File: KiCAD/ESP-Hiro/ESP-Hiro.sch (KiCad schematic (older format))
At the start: 69 parts, among them J1 Conn_Q1, J2 Conn_Q2, J3 Conn_Q3, J4 Conn_Q4, J5 Conn_Q5, J6 Conn_ADC, J7 Korean Hroparts TYPE-C-31-M-12, Q1 AO3400A, Q2 AO3400A, Q3 AO3400A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

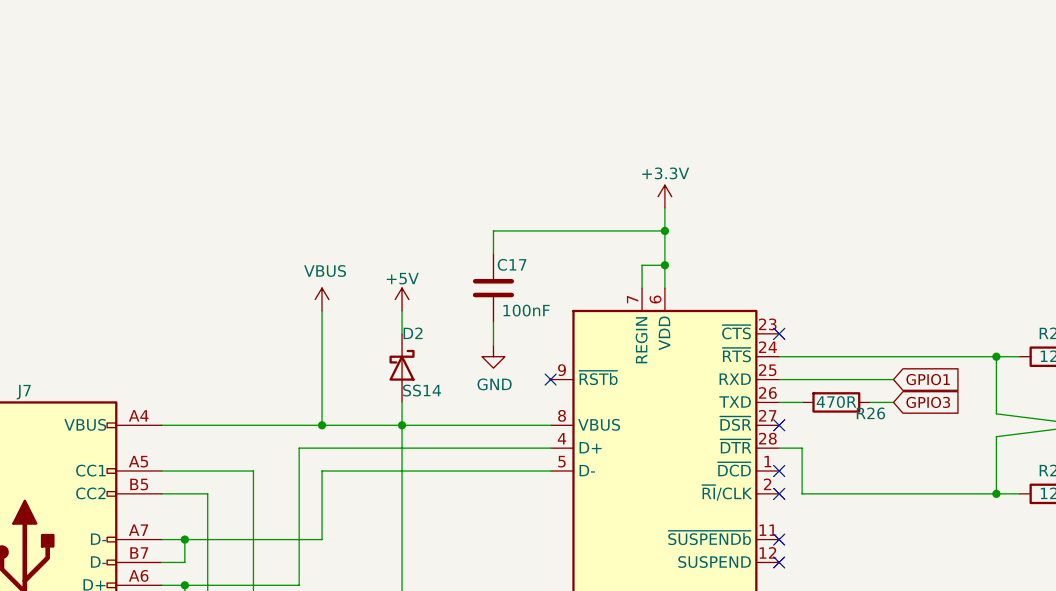
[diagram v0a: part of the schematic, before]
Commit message: configure CP2102 as only USB powered
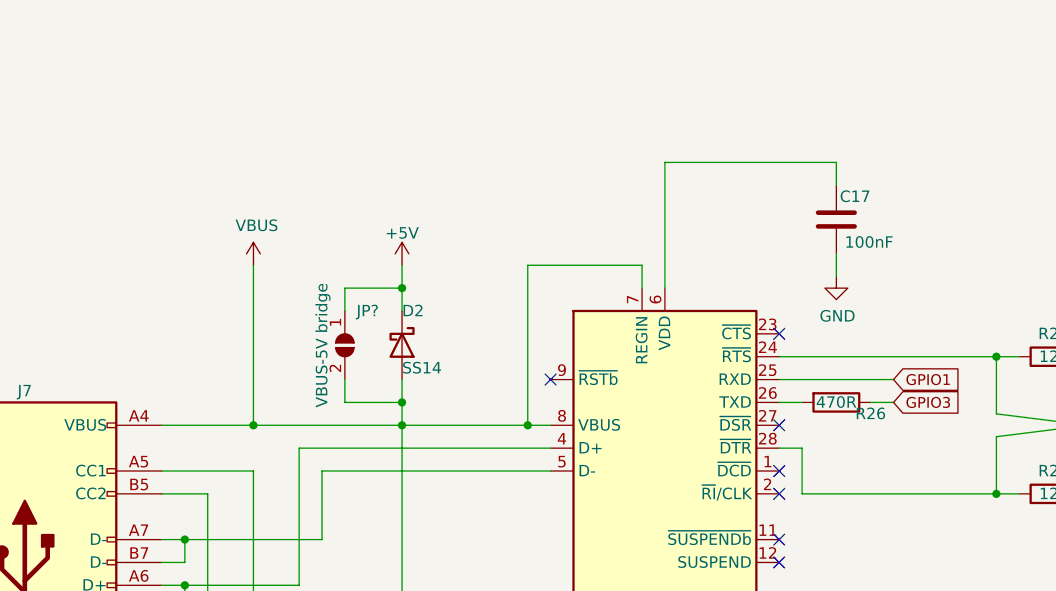
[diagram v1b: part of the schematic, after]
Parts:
- added JP?: VBUS-5V bridge, Jumper:SolderJumper-2_P1.3mm_Open_TrianglePad1.0x1.5mm, symbol Jumper:SolderJumper_2_Open
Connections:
- net +3V3: no longer C17.2, U5.6 (VDD), U5.7 (REGIN)
- net +5V: now also JP?.1 (A)
- net VBUS: now also U5.7 (REGIN), JP?.2 (B)
- new net: C17.2, U5.6 (VDD)
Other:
- moved on the sheet: C17, D2
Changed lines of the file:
@@
 	1200 6750 1200 6850
 Wire Wire Line
-	2100 5150 2800 5150
+	2100 5150 2500 5150
 Wire Wire Line
 	2100 5650 2200 5650
@@
 L power:VBUS #PWR0102
 U 1 1 602A343F
-P 2800 4650
-F 0 "#PWR0102" H 2800 4500 50  0001 C CNN
-F 1 "VBUS" H 2815 4823 50  0000 C CNN
-F 2 "" H 2800 4650 50  0001 C CNN
-F 3 "" H 2800 4650 50  0001 C CNN
-	1    2800 4650
+P 2500 4450
+F 0 "#PWR0102" H 2500 4300 50  0001 C CNN
+F 1 "VBUS" H 2515 4623 50  0000 C CNN
+F 2 "" H 2500 4450 50  0001 C CNN
+F 3 "" H 2500 4450 50  0001 C CNN
+	1    2500 4450
 	1    0    0    -1
 $EndComp
 Connection ~ 3150 5150
 Wire Wire Line
-	3150 5150 3800 5150
-$Comp
-L power:+3.3V #PWR?
-U 1 1 602B1B9F
-P 4300 4200
-AR Path="/601D55C5/602B1B9F" Ref="#PWR?"  Part="1"
-AR Path="/602B1B9F" Ref="#PWR0103"  Part="1"
-F 0 "#PWR0103" H 4300 4050 50  0001 C CNN
-F 1 "+3.3V" H 4300 4350 50  0000 C CNN
-F 2 "" H 4300 4200 50  0001 C CNN
-F 3 "" H 4300 4200 50  0001 C CNN
-	1    4300 4200
-	1    0    0    -1
-$EndComp
-Wire Wire Line
-	4300 4550 4300 4450
-Wire Wire Line
-	4200 4550 4200 4450
-Wire Wire Line
-	4200 4450 4300 4450
-Connection ~ 4300 4450
+	3150 5150 3700 5150
 $Comp
 L power:GND #PWR0104
@@
 L Device:C C?
 U 1 1 602E9F87
-P 3550 4550
+P 5050 4250
 AR Path="/601D55C5/602E9F87" Ref="C?"  Part="1"
 AR Path="/602E9F87" Ref="C17"  Part="1"
-F 0 "C17" H 3400 4450 50  0000 L CNN
-F 1 "100nF" H 3300 4650 50  0000 L CNN
-F 2 "Capacitor_SMD:C_0603_1608Metric" H 3550 4550 50  0001 C CNN
-F 3 "" H 3550 4550 50  0001 C CNN
-F 4 "C14663" V 3550 4550 50  0001 C CNN "LCSC"
-	1    3550 4550
+F 0 "C17" H 4900 4150 50  0000 L CNN
+F 1 "100nF" H 4800 4350 50  0000 L CNN
+F 2 "Capacitor_SMD:C_0603_1608Metric" H 5050 4250 50  0001 C CNN
+F 3 "" H 5050 4250 50  0001 C CNN
+F 4 "C14663" V 5050 4250 50  0001 C CNN "LCSC"
+	1    5050 4250
 	-1   0    0    1
 $EndComp
@@
 L power:GND #PWR0105
 U 1 1 603027BC
-P 3550 4800
-F 0 "#PWR0105" H 3550 4550 50  0001 C CNN
-F 1 "GND" H 3555 4627 50  0000 C CNN
-F 2 "" H 3550 4800 50  0001 C CNN
-F 3 "" H 3550 4800 50  0001 C CNN
-	1    3550 4800
-	1    0    0    -1
-$EndComp
-Wire Wire Line
-	3550 4700 3550 4800
+P 5050 4500
+F 0 "#PWR0105" H 5050 4250 50  0001 C CNN
+F 1 "GND" H 5055 4327 50  0000 C CNN
+F 2 "" H 5050 4500 50  0001 C CNN
+F 3 "" H 5050 4500 50  0001 C CNN
+	1    5050 4500
+	1    0    0    -1
+$EndComp
+Wire Wire Line
+	5050 4400 5050 4500
 Wire Wire Line
 	3150 6500 3150 6400
@@
 L MeineBibli:SS14 D2
 U 1 1 6057A53A
-P 3150 4900
-F 0 "D2" V 3000 4900 50  0000 L CNN
-F 1 "SS14" V 3250 4900 50  0000 L CNN
-F 2 "Diode_SMD:D_SMA" H 3150 4725 50  0001 C CNN
-F 3 "https://datasheet.lcsc.com/szlcsc/1903051003_MDD-Jiangsu-Yutai-Elec-SS14_C2480.pdf" H 3150 4900 50  0001 C CNN
-F 4 "C2480" V 3241 4980 50  0001 L CNN "LCSC"
-	1    3150 4900
+P 3150 4800
+F 0 "D2" V 3000 4800 50  0000 L CNN
+F 1 "SS14" V 3250 4800 50  0000 L CNN
+F 2 "Diode_SMD:D_SMA" H 3150 4625 50  0001 C CNN
+F 3 "https://datasheet.lcsc.com/szlcsc/1903051003_MDD-Jiangsu-Yutai-Elec-SS14_C2480.pdf" H 3150 4800 50  0001 C CNN
+F 4 "C2480" V 3241 4880 50  0001 L CNN "LCSC"
+	1    3150 4800
 	0    1    1    0
 $EndComp
-Connection ~ 2800 5150
-Wire Wire Line
-	2800 5150 3150 5150
+Connection ~ 2500 5150
+Wire Wire Line
+	2500 5150 3150 5150
 $Comp
 L power:+5V #PWR?
 U 1 1 60630B5B
-P 3150 4650
+P 3150 4450
 AR Path="/601D55C5/60630B5B" Ref="#PWR?"  Part="1"
 AR Path="/60630B5B" Ref="#PWR0107"  Part="1"
-F 0 "#PWR0107" H 3150 4500 50  0001 C CNN
-F 1 "+5V" H 3150 4790 50  0000 C CNN
-F 2 "" H 3150 4650 50  0001 C CNN
-F 3 "" H 3150 4650 50  0001 C CNN
-	1    3150 4650
-	1    0    0    -1
-$EndComp
-Wire Wire Line
-	3150 4650 3150 4750
-Wire Wire Line
-	2800 4650 2800 5150
+F 0 "#PWR0107" H 3150 4300 50  0001 C CNN
+F 1 "+5V" H 3150 4590 50  0000 C CNN
+F 2 "" H 3150 4450 50  0001 C CNN
+F 3 "" H 3150 4450 50  0001 C CNN
+	1    3150 4450
+	1    0    0    -1
+$EndComp
+Wire Wire Line
+	3150 4450 3150 4550
+Wire Wire Line
+	2500 4450 2500 5150
 Wire Wire Line
 	3150 5150 3150 5050
@@
 	2500 6900 2400 6900
 Connection ~ 2400 6900
-Wire Wire Line
-	3550 4400 3550 4300
-Wire Wire Line
-	3550 4300 4300 4300
-Connection ~ 4300 4300
-Wire Wire Line
-	4300 4300 4300 4450
-Wire Wire Line
-	4300 4200 4300 4300
 $Comp
 L Device:C C16
@@
 Wire Wire Line
 	3150 6400 3150 5150
+$Comp
+L Jumper:SolderJumper_2_Open JP?
+U 1 1 609E58BA
+P 2900 4800
+F 0 "JP?" V 2750 4900 50  0000 C CNN
+F 1 "VBUS-5V bridge" H 2900 4700 50  0000 C CNN
+F 2 "Jumper:SolderJumper-2_P1.3mm_Open_TrianglePad1.0x1.5mm" H 2900 4800 50  0001 C CNN
+F 3 "~" H 2900 4800 50  0001 C CNN
+	1    2900 4800
+	0    1    1    0
+$EndComp
+Wire Wire Line
+	2900 4650 2900 4550
+Wire Wire Line
+	2900 4550 3150 4550
+Connection ~ 3150 4550
+Wire Wire Line
+	3150 4550 3150 4650
+Wire Wire Line
+	2900 4950 2900 5050
+Wire Wire Line
+	2900 5050 3150 5050
+Connection ~ 3150 5050
+Wire Wire Line
+	3150 5050 3150 4950
+Wire Wire Line
+	3700 5150 3700 4450
+Wire Wire Line
+	3700 4450 4200 4450
+Wire Wire Line
+	4200 4450 4200 4550
+Connection ~ 3700 5150
+Wire Wire Line
+	3700 5150 3800 5150
+Wire Wire Line
+	4300 4000 5050 4000
+Wire Wire Line
+	5050 4000 5050 4100
+Wire Wire Line
+	4300 4000 4300 4550
 $EndSCHEMATC

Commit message: Add CP2102 schematic and shift stuff in schematic
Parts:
- gave numbers to parts that had none: 1
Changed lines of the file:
@@
 	3150 6400 3150 5150
 $Comp
-L Jumper:SolderJumper_2_Open JP?
+L Jumper:SolderJumper_2_Open JP2
 U 1 1 609E58BA
 P 2900 4800
-F 0 "JP?" V 2750 4900 50  0000 C CNN
+F 0 "JP2" V 2750 4900 50  0000 C CNN
 F 1 "VBUS-5V bridge" H 2900 4700 50  0000 C CNN
 F 2 "Jumper:SolderJumper-2_P1.3mm_Open_TrianglePad1.0x1.5mm" H 2900 4800 50  0001 C CNN
